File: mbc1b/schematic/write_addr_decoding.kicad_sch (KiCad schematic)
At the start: 6 parts

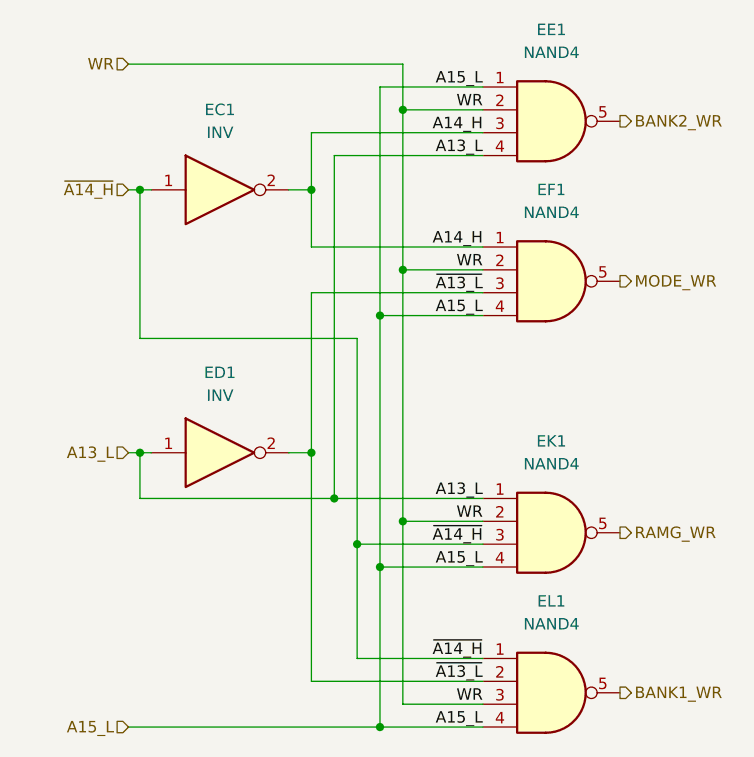
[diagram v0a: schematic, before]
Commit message: Update MBC1B schematic with latest kingfish compatibility
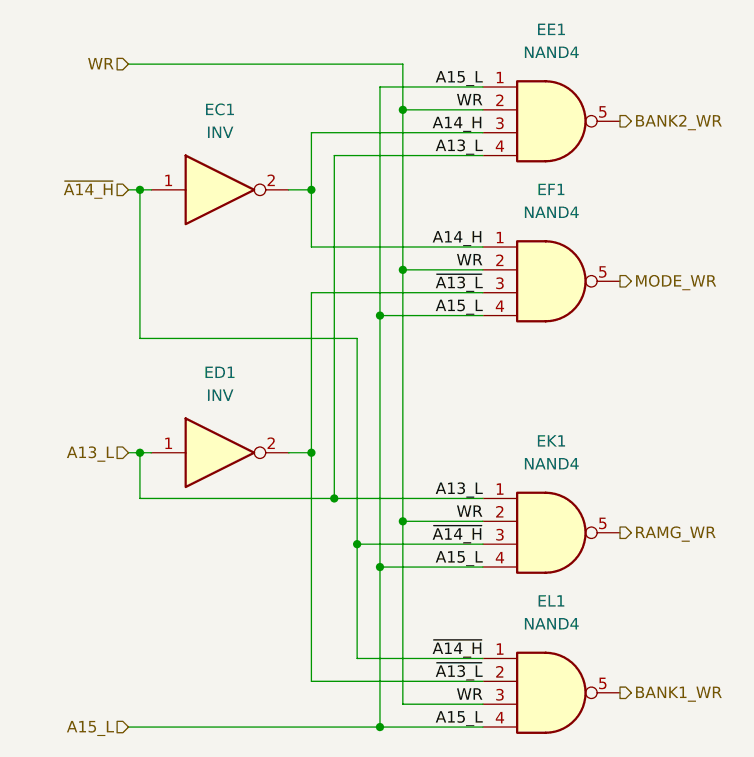
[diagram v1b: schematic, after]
